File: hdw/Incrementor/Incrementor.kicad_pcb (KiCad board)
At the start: 4 copper layers, 94.3 x 49.9 mm, 226 parts, among them J1901 CLK_OUT, J201 +12V IN, J801 CLK_IN, SW701 Cap_Touch, SW702 Cap_Touch, SW703 Cap_Touch, U1001 4026, U1002 HDSP-7503, U1101 4026, U1102 HDSP-7503, U1201 4026, U1202 HDSP-7503, U1301 4026, U1302 HDSP-7503, U1401 4026, U1402 HDSP-7503, U1501 4026, U1502 HDSP-7503, U1601 4026, U1602 HDSP-7503, U1701 4026, U1702 HDSP-7503, U1801 4026, U1802 HDSP-7503, U1901 74LVC1G17, U201 TPS26600RHFT, U301 TPS62130, U401 CD4024, U402 CD4040, U501 74LVC1G08, U502 74LVC1G08, U503 74LVC1G08, U504 74LVC1G08, U505 74LVC1G08, U506 74LVC1G08, U507 4072, U508 4017, U601 74LVC1G06, U602 74LVC1G06, U603 74LVC1G06, U604 74LVC1G06, U605 74LVC1G06, U606 74LVC1G06, U607 74LVC1G06, U608 74LVC1G06, U609 74LVC1G06, U701 AT42QT1010-TSHR, U702 TLV71330PDBV, U703 TLV71330PDBV, U704 74LVC1G80, U705 74LVC1G17, U706 TLV71330PDBV, U707 AT42QT1010-TSHR, U708 AT42QT1010-TSHR, U709 74LVC1G17, U710 74LVC1G17, U801 74LVC1G17, U901 4026, U902 HDSP-7503, X401 SG-3030CM

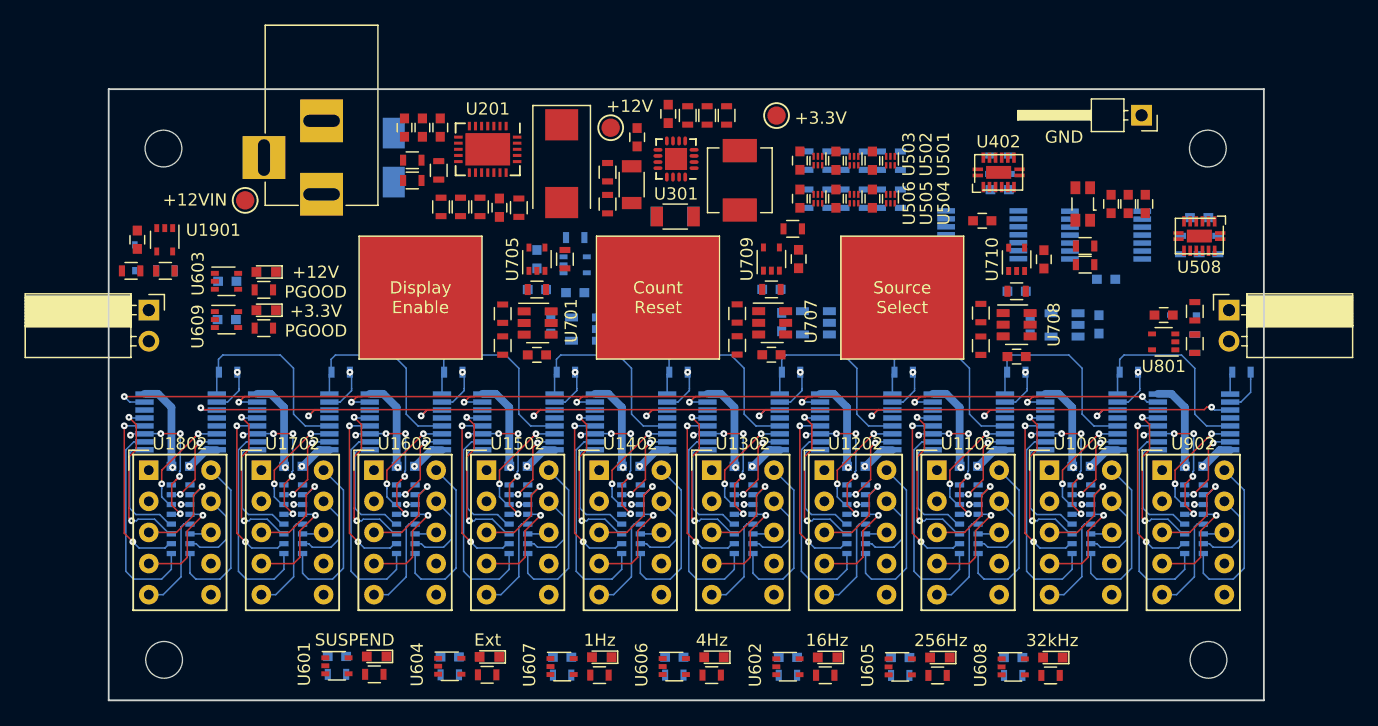
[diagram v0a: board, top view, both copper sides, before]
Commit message: Started routing, fixed AND gate pinout
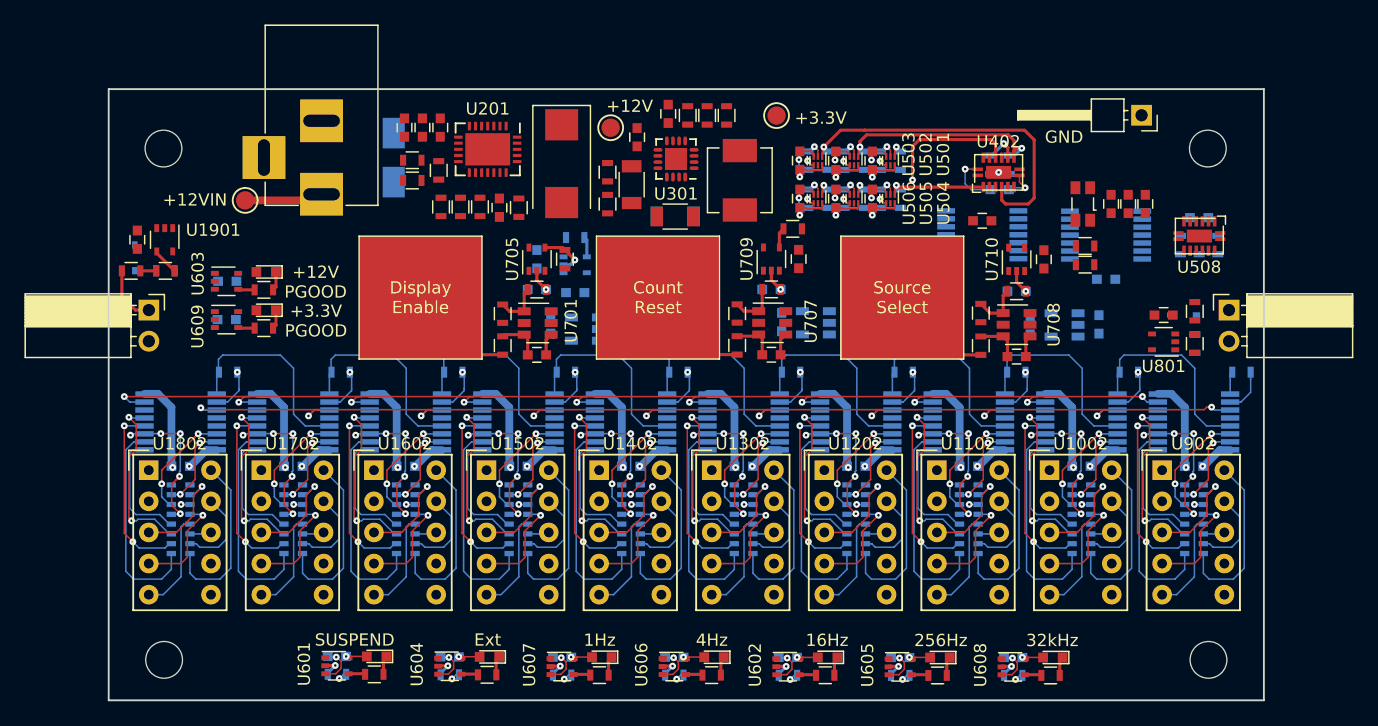
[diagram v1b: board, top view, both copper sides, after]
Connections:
- U501 pad 5: +3V3 -> Net-(U501-Pad5)
- U501 pad 6: (no net) -> +3V3
- U502 pad 5: +3V3 -> Net-(U502-Pad5)
- U502 pad 6: (no net) -> +3V3
- U503 pad 5: +3V3 -> Net-(U503-Pad5)
- U503 pad 6: (no net) -> +3V3
- U504 pad 5: +3V3 -> Net-(U504-Pad5)
- U504 pad 6: (no net) -> +3V3
- U505 pad 5: +3V3 -> Net-(U505-Pad5)
- U505 pad 6: (no net) -> +3V3
- U506 pad 5: +3V3 -> Net-(U506-Pad5)
- U506 pad 6: (no net) -> +3V3
- U508 pad 17: GND -> (no net)
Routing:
- net GND: track 65.6 -> 131.6 mm, vias 19 -> 41
- net +3V3: track 76.1 -> 110.3 mm, vias 10 -> 24
- net 16Hz_Clock: track 0.00 -> 28.2 mm, vias 0 -> 1
- net 256Hz_Clock: track 0.00 -> 18.1 mm, vias 0 -> 2
- net 1Hz_Clock: track 0.00 -> 16.9 mm, vias 0 -> 2
- net Net-(R701-Pad1): track 0.00 -> 8.64 mm
- net 4Hz_Clock: track 0.00 -> 8.47 mm, vias 0 -> 1
- net Net-(R702-Pad1): track 0.00 -> 8.39 mm
- net Net-(R703-Pad1): track 0.00 -> 8.35 mm
- net +12Vin: track 0.00 -> 6.44 mm
- net Net-(J1901-Pad1): track 0.00 -> 4.76 mm
- net Count_Reset: track 106.9 -> 111.3 mm, vias 10 -> 11
- net Net-(R707-Pad1): track 0.00 -> 4.06 mm
- net Net-(R711-Pad1): track 0.00 -> 3.96 mm, vias 0 -> 1
- net Net-(R704-Pad1): track 0.00 -> 3.89 mm
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- added copper zone on GND, net GND
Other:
- net class Signal: trace_width 0.127 -> 0.254

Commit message: lots more routing
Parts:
- moved C401 6.20 mm to (155.8, 74.0), turned to 0 degrees
- moved C402 4.48 mm to (155.8, 72.6), turned to 0 degrees
- moved C403 3.09 mm to (155.8, 71.2), turned to 0 degrees
- moved X401 3.06 mm to (155.8, 68.9), turned to 0 degrees
- moved D201 1.73 mm to (94.8, 64.3)
- moved C508 0.94 mm to (161.4, 69.3)
- moved R513 0.94 mm to (161.4, 71.5)
- moved R514 0.94 mm to (159.8, 71.5)
- moved R515 0.94 mm to (162.9, 71.5)
- moved U508 0.94 mm to (161.4, 70.8)
- moved R302 0.54 mm to (113.9, 66.1)
- moved R303 0.54 mm to (113.9, 68.7)
- turned C704 to 270 degrees
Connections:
- U508 pad 17: (no net) -> GND
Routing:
- net GND: track 131.6 -> 252.0 mm, vias 41 -> 93
- net +3V3: track 110.3 -> 191.9 mm, vias 24 -> 67
- net 1Hz_Clock_Select: track 3.39 -> 48.8 mm, vias 2 -> 3
- net 16Hz_Clock_Select: track 3.39 -> 44.1 mm, vias 2 -> 3
- net 4Hz_Clock_Select: track 3.39 -> 40.1 mm, vias 2 -> 4
- net 32768Hz_Clock_Select: track 3.39 -> 37.3 mm, vias 2 -> 3
- net Count_Reset: track 111.3 -> 140.3 mm, vias 11 -> 13
- net Net-(U502-Pad4): track 0.64 -> 28.3 mm, vias 1 -> 2
- net +12Vin: track 6.44 -> 30.7 mm
- net Stage01_Clock_In: track 1.86 -> 26.1 mm
- net Source_Select: track 0.00 -> 22.9 mm, vias 0 -> 1
- net Net-(U505-Pad4): track 0.64 -> 21.4 mm, vias 1 -> 3
- net Net-(U506-Pad4): track 0.64 -> 21.0 mm, vias 1 -> 2
- net Net-(U503-Pad4): track 0.64 -> 20.6 mm, vias 1 -> 2
- net Display_Enable: track 111.1 -> 130.6 mm
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- added copper zone on F.Cu, net +12V
- added copper zone on F.Cu, net +12Vin
- added copper zone on B.Cu, net +3V3
- added copper zone on F.Cu, net +3V3
- added copper zone on PWR, net +3V3
- added copper zone on F.Cu, net GND
- added copper zone on B.Cu, net Net-(C204-Pad2)
- added copper zone on GND, net Net-(C204-Pad2)
- added copper zone on F.Cu, net Net-(L301-Pad1)
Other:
- net class Default: trace_width 0.127 -> 0.254

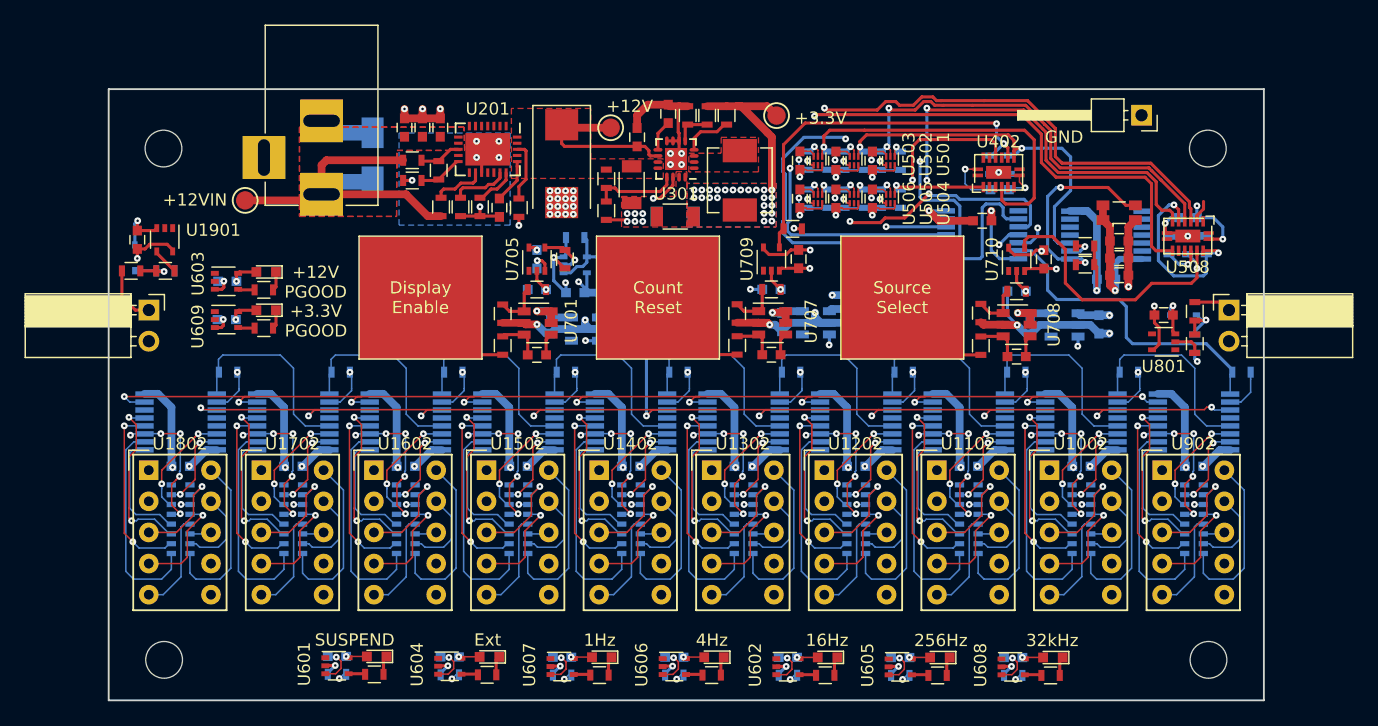
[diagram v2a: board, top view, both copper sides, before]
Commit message: Finished first pass on routing
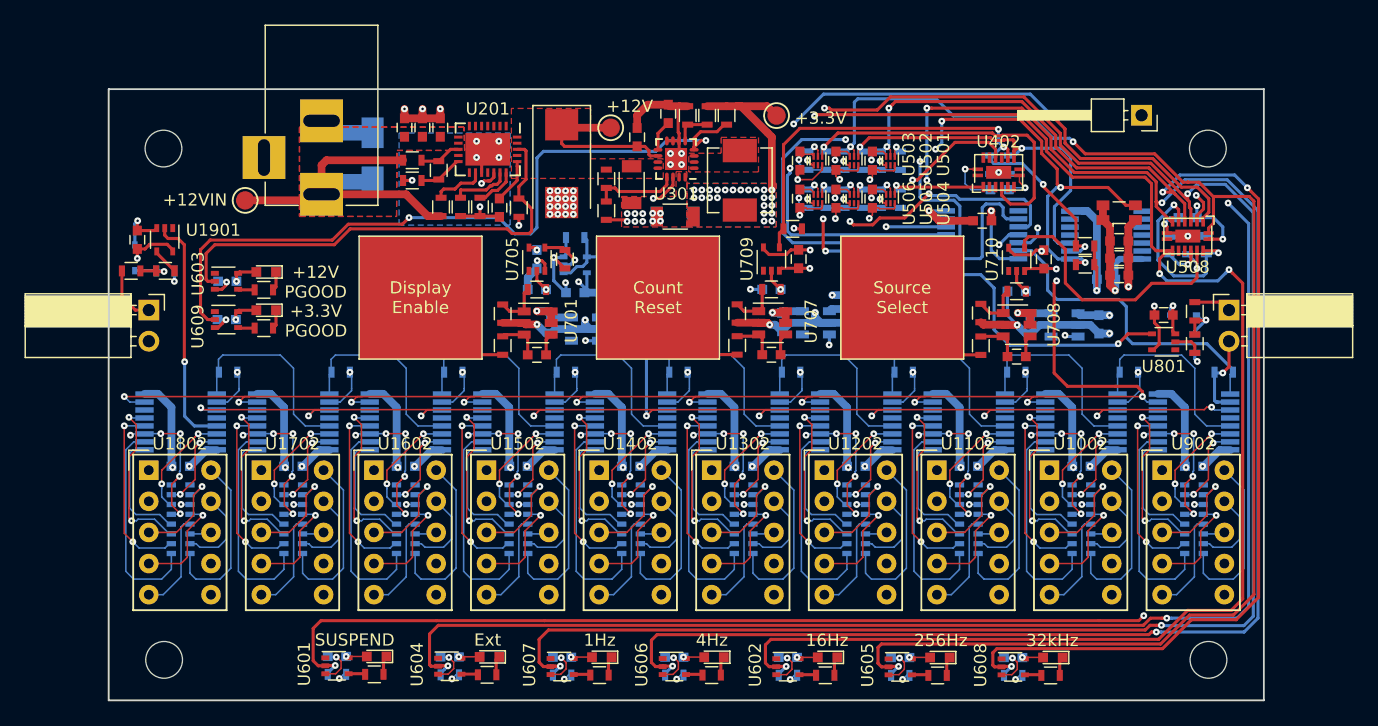
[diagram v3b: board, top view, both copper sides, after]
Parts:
- moved R901 1.45 mm to (164.3, 81.9), turned to 180 degrees
- moved R503 0.15 mm to (131.9, 64.6)
- moved R506 0.15 mm to (131.9, 67.7)
- moved R502 0.15 mm to (134.8, 64.6)
- moved R505 0.15 mm to (134.8, 67.7)
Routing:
- net External_Clock_Select: track 3.39 -> 181.8 mm, vias 2 -> 6
- net Suspend: track 3.64 -> 127.5 mm, vias 1 -> 3
- net 256Hz_Clock_Select: track 3.39 -> 113.3 mm, vias 2 -> 3
- net 1Hz_Clock_Select: track 48.8 -> 150.0 mm, vias 3 -> 5
- net 4Hz_Clock_Select: track 40.1 -> 135.6 mm, vias 4 -> 6
- net 16Hz_Clock_Select: track 44.1 -> 122.5 mm, vias 3 -> 5
- net 32768Hz_Clock_Select: track 37.3 -> 104.6 mm, vias 3 -> 5
- net POS3P3_PGOOD: track 4.06 -> 61.1 mm, vias 0 -> 2
- net External_Clock: track 1.31 -> 39.0 mm, vias 1 -> 4
- net POS12_PGOOD: track 4.91 -> 38.7 mm
- net Count_Reset: track 140.3 -> 171.6 mm, vias 13 -> 15
- net Stage10_Clock_Out: track 0.00 -> 19.5 mm, vias 0 -> 1
- net 32768Hz_Clock: track 18.0 -> 37.2 mm, vias 3 -> 5
- net GND: track 252.0 -> 264.4 mm, vias 93 -> 99
- net +3V3: track 191.9 -> 195.1 mm, vias 67 -> 68
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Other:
- board text removed: "GND"

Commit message: Added lots of PCB symbols/features
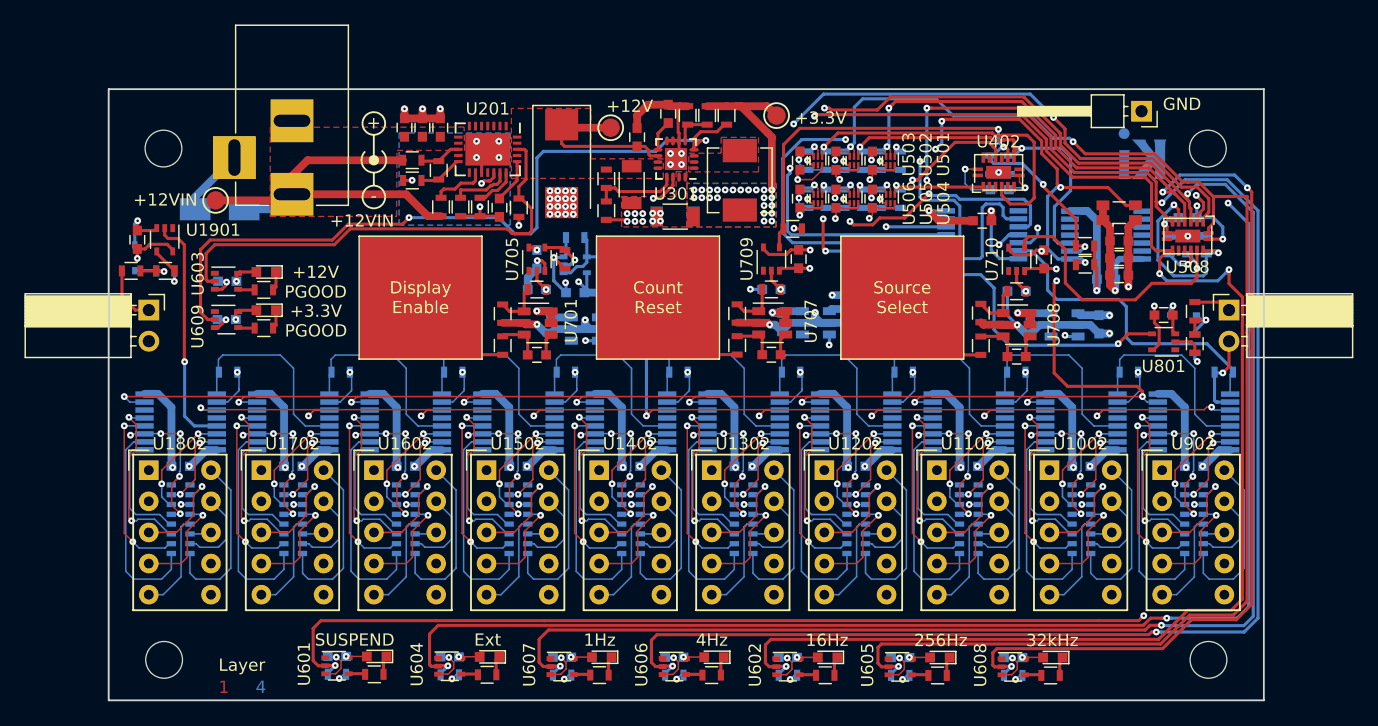
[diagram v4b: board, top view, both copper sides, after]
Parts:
- added G***: Owl_1_Logo, Custom Footprints Library:Owl_1_Logo, B.Cu at (123.8, 71.6)
- added G***: LOGO, Custom Footprints Library:incrementor_qr_code, B.Cu at (98.5, 72.3)
- added REF**: KiCAD Logo, Symbol:Symbol_KiCAD-Logo_CopperAndSilkScreenTop, B.Cu at (154.0, 64.3)
- added REF**: Symbol_Barrel_Polarity, Symbol:Symbol_Barrel_Polarity, F.Cu at (94.9, 64.6)
- moved D201 13.2 mm to (82.4, 68.6), turned to 180 degrees
- moved J201 2.41 mm to (88.3, 67.4)
- moved TP202 2.41 mm to (82.0, 67.9)
- moved TP201 0.33 mm to (157.6, 60.6)
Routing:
- net +12Vin: track 30.7 -> 34.9 mm
- net GND: track 264.4 -> 265.4 mm
- net 256Hz_Clock_Select: track 113.3 -> 112.6 mm
- net External_Clock_Select: track 181.8 -> 181.1 mm
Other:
- board text added: "+"
- board text added: "-"
- board text added: "1"
- board text added: "2"
- board text added: "3"
- board text added: "4"
- board text added: "GND"
- board text added: "Incrementor Rev A 2019"
- board text added: "JLCJLCJLCJLC"
- board text added: "Layer"

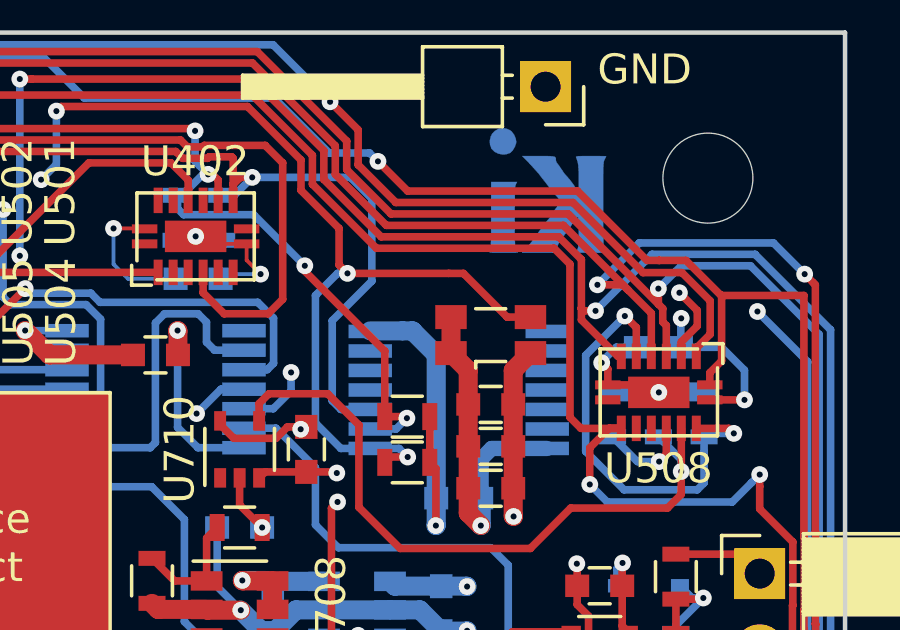
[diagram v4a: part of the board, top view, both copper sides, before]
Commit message: Fixed a few BOM issues
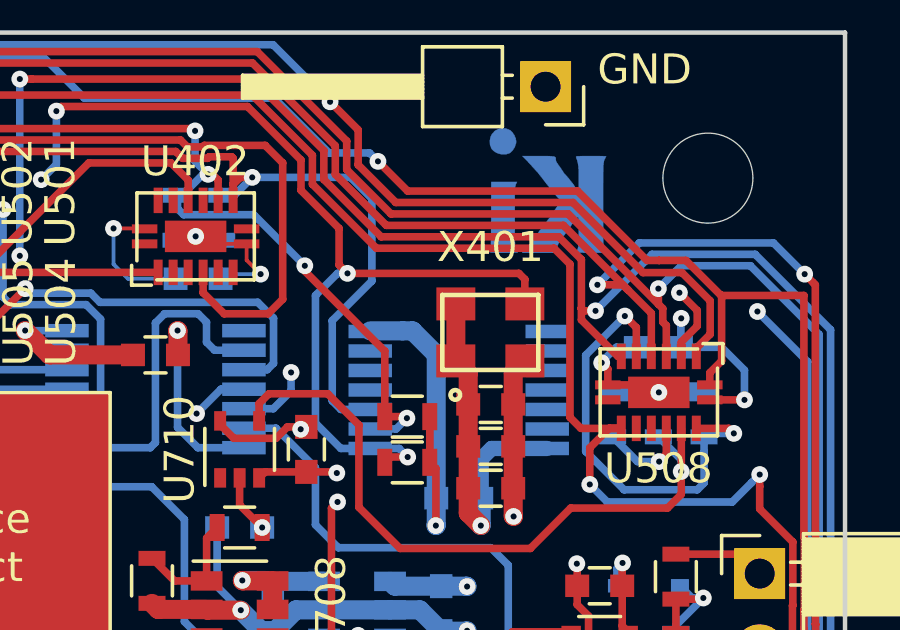
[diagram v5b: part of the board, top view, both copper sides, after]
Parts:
- X401: value SG-3030CM -> ECS-327KE; footprint Oscillator:Oscillator_SMD_SeikoEpson_SG3030CM -> Custom Footprints Library:ECS-327KE
- moved X401 0.09 mm to (155.8, 68.8)

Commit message: Fixed issues, generated gerbers
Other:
- board text added: "CLK IN"
- board text added: "CLK OUT"
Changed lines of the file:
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@@
   (general
     (thickness 1.6)
-    (drawings 34)
+    (drawings 36)
     (tracks 3027)
     (zones 0)
@@
       (psa4output false)
       (plotreference true)
-      (plotvalue true)
+      (plotvalue false)
       (plotinvisibletext false)
       (padsonsilk false)
@@
       (outputformat 1)
       (mirror false)
-      (drillshape 1)
+      (drillshape 0)
       (scaleselection 1)
-      (outputdirectory ""))
+      (outputdirectory "gerbers/"))
   )
   (net 0 "")
@@
     (fp_line (start 1.6 1.25) (end -1.6 1.25) (layer F.SilkS) (width 0.1524))
     (fp_line (start -1.6 1.25) (end -1.6 -1.25) (layer F.SilkS) (width 0.1524))
-    (fp_circle (center -1.1684 2.0828) (end -1.016 2.032) (layer F.SilkS) (width 0.1524))
+    (fp_circle (center -2.0066 1.8542) (end -1.9304 1.8542) (layer F.SilkS) (width 0.1524))
     (pad 4 smd rect (at -1.15 -0.95) (size 1.3 1.1) (layers F.Cu F.Paste F.Mask)
       (net 6 +3V3))
@@
     )
   )
-  (gr_text GND (at 160.909 60.0075) (layer F.SilkS)
+  (gr_text "CLK\nOUT" (at 76.581 83.5025) (layer F.SilkS)
+    (effects (font (size 1 1) (thickness 0.15)))
+  )
+  (gr_text "CLK\nIN" (at 164.7825 83.5025) (layer F.SilkS)
+    (effects (font (size 1 1) (thickness 0.15)))
+  )
+  (gr_text GND (at 150.876 62.357) (layer F.SilkS)
     (effects (font (size 1 1) (thickness 0.15)))
   )
